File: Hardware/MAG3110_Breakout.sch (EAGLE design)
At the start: 17 parts, among them U1 MAG31101:1

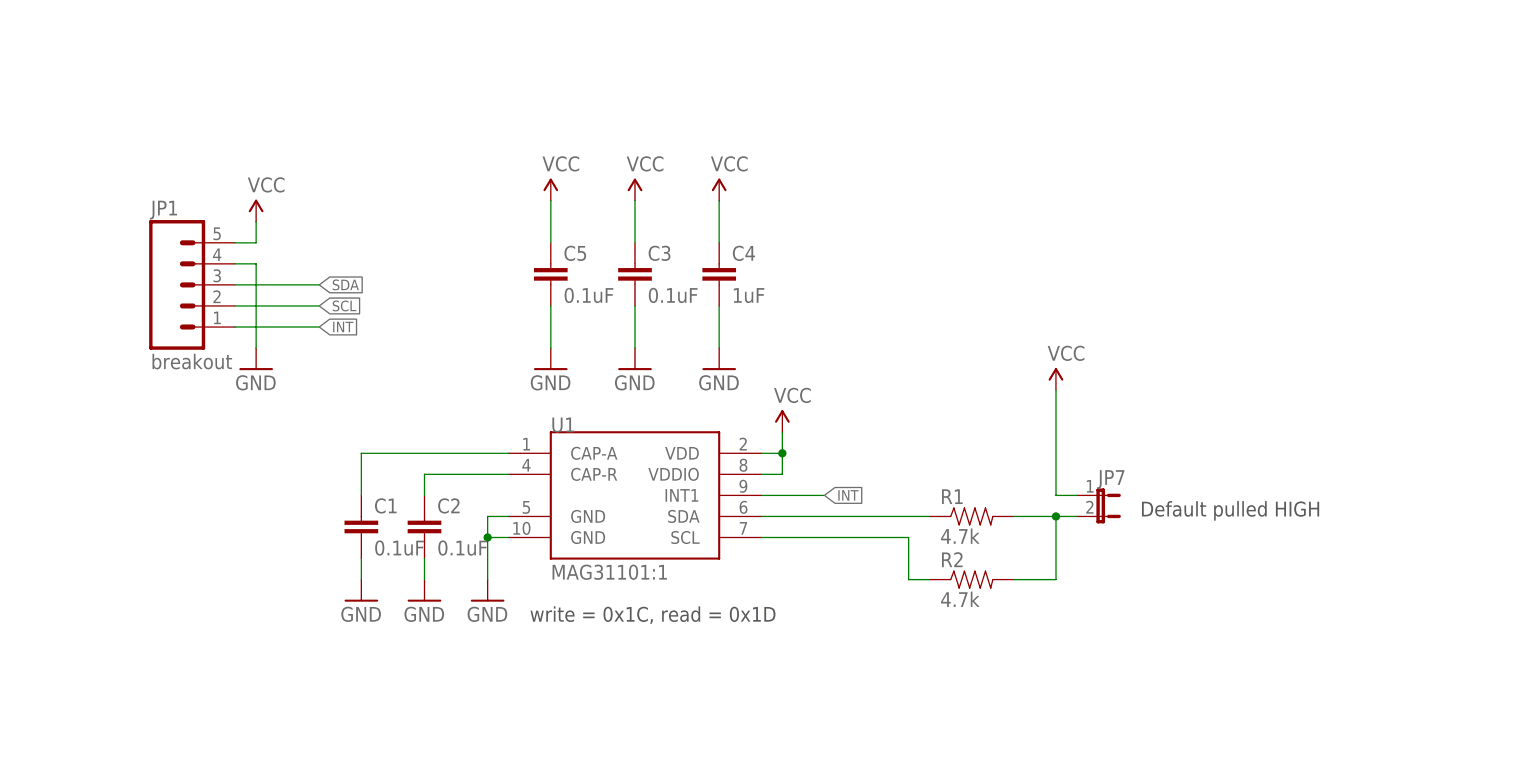
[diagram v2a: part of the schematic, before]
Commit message: Modified I2C pullup solder jumper
Changed solder jumper for I2C pullup so that I2C lines will be
completely floating if jumper is open. Moved capacitor bank to the left
.005 grid spaces and moved resistors and cap on right side over .005 to
the right, all for better trace routing. Changed int trace to be more
direct to header.
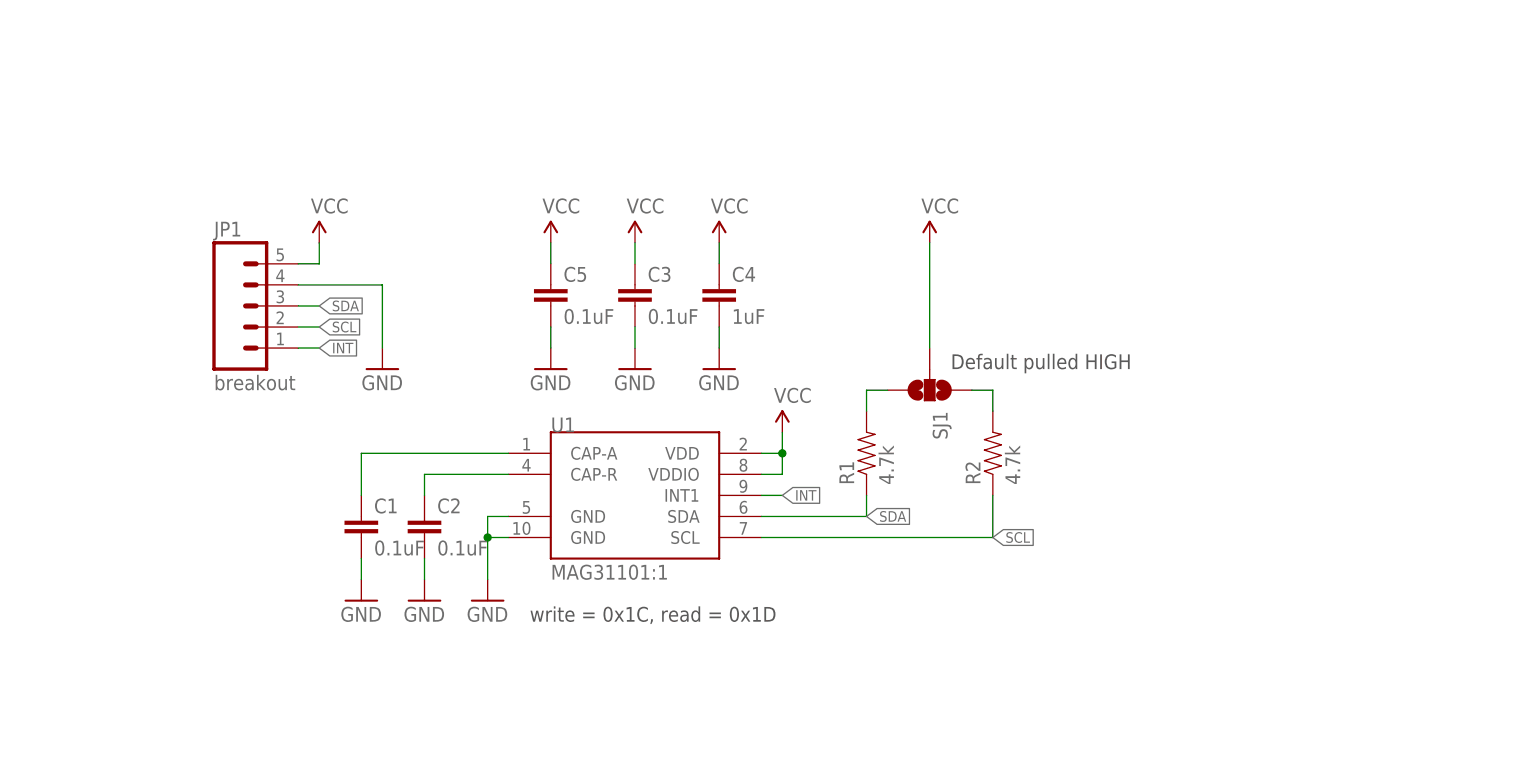
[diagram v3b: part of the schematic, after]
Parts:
- removed JP7: (no value), SparkFun-Passives:JUMPER-2SMD-NC
- added SJ1: (no value), SparkFun-Passives:SOLDERJUMPER_2WAYPASTE1&2&3
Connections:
- new net N$4: R1.2, SJ1.3
- net N$3: now also SJ1.1; no longer JP7.2, R1.2
- net VCC: now also SJ1.2; no longer JP7.1
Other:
- moved on the sheet: C3, C4, C5, JP1, R1, R2
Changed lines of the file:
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@@
 <?xml version="1.0" encoding="utf-8"?>
 <!DOCTYPE eagle SYSTEM "eagle.dtd">
-<eagle version="6.4">
+<eagle version="6.5.0">
 <drawing>
 <settings>
@@
 <part name="GND7" library="SparkFun" deviceset="GND" device=""/>
 <part name="GND8" library="SparkFun" deviceset="GND" device=""/>
-<part name="JP7" library="SparkFun-Passives" deviceset="JUMPER-2" device="SMD-NC"/>
+<part name="SJ1" library="SparkFun-Passives" deviceset="SOLDERJUMPER_2WAY" device="PASTE1&amp;2&amp;3"/>
 </parts>
 <sheets>
@@
 <text x="241.3" y="7.62" size="2.54" layer="94" ratio="15">12</text>
 <text x="167.64" y="10.16" size="2.54" layer="94" ratio="15">Kade Jensen</text>
-<text x="185.42" y="83.82" size="1.778" layer="97">Default pulled HIGH</text>
+<text x="162.56" y="101.6" size="1.778" layer="97">Default pulled HIGH</text>
 </plain>
 <instances>
@@
 <instance part="GND2" gate="1" x="91.44" y="73.66"/>
 <instance part="GND3" gate="1" x="99.06" y="73.66"/>
-<instance part="C3" gate="G$1" x="124.46" y="111.76"/>
-<instance part="C4" gate="G$1" x="134.62" y="111.76"/>
-<instance part="P+1" gate="1" x="124.46" y="121.92"/>
+<instance part="C3" gate="G$1" x="124.46" y="109.22"/>
+<instance part="C4" gate="G$1" x="134.62" y="109.22"/>
+<instance part="P+1" gate="1" x="124.46" y="116.84"/>
 <instance part="GND4" gate="1" x="124.46" y="101.6"/>
 <instance part="P+2" gate="1" x="142.24" y="93.98"/>
-<instance part="C5" gate="G$1" x="114.3" y="111.76"/>
-<instance part="R1" gate="G$1" x="165.1" y="83.82"/>
-<instance part="R2" gate="G$1" x="165.1" y="76.2"/>
-<instance part="P+3" gate="1" x="175.26" y="99.06"/>
-<instance part="JP1" gate="G$1" x="68.58" y="111.76"/>
-<instance part="P+4" gate="1" x="78.74" y="119.38"/>
-<instance part="GND5" gate="1" x="78.74" y="101.6"/>
+<instance part="C5" gate="G$1" x="114.3" y="109.22"/>
+<instance part="R1" gate="G$1" x="152.4" y="91.44" rot="R90"/>
+<instance part="R2" gate="G$1" x="167.64" y="91.44" rot="R90"/>
+<instance part="P+3" gate="1" x="160.02" y="116.84"/>
+<instance part="JP1" gate="G$1" x="76.2" y="109.22"/>
+<instance part="P+4" gate="1" x="86.36" y="116.84"/>
+<instance part="GND5" gate="1" x="93.98" y="101.6"/>
 <instance part="JP2" gate="G$1" x="246.38" y="25.4"/>
 <instance part="JP3" gate="G$1" x="246.38" y="33.02"/>
@@
 <instance part="FRAME2" gate="G$2" x="147.32" y="0"/>
 <instance part="LOGO1" gate="G$1" x="15.24" y="12.7"/>
-<instance part="P+5" gate="1" x="114.3" y="121.92"/>
-<instance part="P+6" gate="1" x="134.62" y="121.92"/>
+<instance part="P+5" gate="1" x="114.3" y="116.84"/>
+<instance part="P+6" gate="1" x="134.62" y="116.84"/>
 <instance part="GND7" gate="1" x="114.3" y="101.6"/>
 <instance part="GND8" gate="1" x="134.62" y="101.6"/>
-<instance part="JP7" gate="A" x="180.34" y="86.36" rot="R270"/>
+<instance part="SJ1" gate="G$1" x="160.02" y="99.06" rot="R270"/>
 </instances>
 <busses>
@@
 </segment>
 <segment>
-<wire x1="124.46" y1="104.14" x2="124.46" y2="109.22" width="0.1524" layer="91"/>
+<wire x1="124.46" y1="104.14" x2="124.46" y2="106.68" width="0.1524" layer="91"/>
 <pinref part="C3" gate="G$1" pin="2"/>
 <pinref part="GND4" gate="1" pin="GND"/>
 </segment>
 <segment>
-<wire x1="76.2" y1="114.3" x2="78.74" y2="114.3" width="0.1524" layer="91"/>
-<wire x1="78.74" y1="114.3" x2="78.74" y2="104.14" width="0.1524" layer="91"/>
+<wire x1="83.82" y1="111.76" x2="93.98" y2="111.76" width="0.1524" layer="91"/>
+<wire x1="93.98" y1="111.76" x2="93.98" y2="104.14" width="0.1524" layer="91"/>
 <pinref part="JP1" gate="G$1" pin="4"/>
 <pinref part="GND5" gate="1" pin="GND"/>
@@
 <pinref part="C4" gate="G$1" pin="2"/>
 <pinref part="GND8" gate="1" pin="GND"/>
-<wire x1="134.62" y1="109.22" x2="134.62" y2="104.14" width="0.1524" layer="91"/>
+<wire x1="134.62" y1="106.68" x2="134.62" y2="104.14" width="0.1524" layer="91"/>
 </segment>
 <segment>
 <pinref part="C5" gate="G$1" pin="2"/>
 <pinref part="GND7" gate="1" pin="GND"/>
-<wire x1="114.3" y1="109.22" x2="114.3" y2="104.14" width="0.1524" layer="91"/>
+<wire x1="114.3" y1="106.68" x2="114.3" y2="104.14" width="0.1524" layer="91"/>
 </segment>
 </net>
 <net name="VCC" class="0">
 <segment>
-<wire x1="124.46" y1="121.92" x2="124.46" y2="116.84" width="0.1524" layer="91"/>
+<wire x1="124.46" y1="116.84" x2="124.46" y2="114.3" width="0.1524" layer="91"/>
 <pinref part="C3" gate="G$1" pin="1"/>
 <pinref part="P+1" gate="1" pin="VCC"/>
@@
 </segment>
 <segment>
-<wire x1="76.2" y1="116.84" x2="78.74" y2="116.84" width="0.1524" layer="91"/>
-<wire x1="78.74" y1="116.84" x2="78.74" y2="119.38" width="0.1524" layer="91"/>
+<wire x1="83.82" y1="114.3" x2="86.36" y2="114.3" width="0.1524" layer="91"/>
+<wire x1="86.36" y1="114.3" x2="86.36" y2="116.84" width="0.1524" layer="91"/>
 <pinref part="JP1" gate="G$1" pin="5"/>
 <pinref part="P+4" gate="1" pin="VCC"/>
@@
 <segment>
 <pinref part="P+3" gate="1" pin="VCC"/>
-<wire x1="175.26" y1="86.36" x2="175.26" y2="99.06" width="0.1524" layer="91"/>
-<pinref part="JP7" gate="A" pin="1"/>
-<wire x1="177.8" y1="86.36" x2="175.26" y2="86.36" width="0.1524" layer="91"/>
+<wire x1="160.02" y1="104.14" x2="160.02" y2="116.84" width="0.1524" layer="91"/>
+<pinref part="SJ1" gate="G$1" pin="2"/>
 </segment>
 <segment>
 <pinref part="C5" gate="G$1" pin="1"/>
 <pinref part="P+5" gate="1" pin="VCC"/>
-<wire x1="114.3" y1="116.84" x2="114.3" y2="121.92" width="0.1524" layer="91"/>
+<wire x1="114.3" y1="114.3" x2="114.3" y2="116.84" width="0.1524" layer="91"/>
 </segment>
 <segment>
 <pinref part="C4" gate="G$1" pin="1"/>
 <pinref part="P+6" gate="1" pin="VCC"/>
-<wire x1="134.62" y1="121.92" x2="134.62" y2="116.84" width="0.1524" layer="91"/>
+<wire x1="134.62" y1="116.84" x2="134.62" y2="114.3" width="0.1524" layer="91"/>
 </segment>
 </net>
 <net name="SDA" class="0">
 <segment>
-<wire x1="139.7" y1="83.82" x2="160.02" y2="83.82" width="0.1524" layer="91"/>
+<wire x1="83.82" y1="109.22" x2="86.36" y2="109.22" width="0.1524" layer="91"/>
+<pinref part="JP1" gate="G$1" pin="3"/>
+<label x="86.36" y="109.22" size="1.27" layer="95" xref="yes"/>
+</segment>
+<segment>
+<pinref part="R1" gate="G$1" pin="1"/>
+<wire x1="152.4" y1="86.36" x2="152.4" y2="83.82" width="0.1524" layer="91"/>
 <pinref part="U1" gate="G$1" pin="SDA"/>
-<pinref part="R1" gate="G$1" pin="1"/>
-</segment>
-<segment>
-<wire x1="76.2" y1="111.76" x2="86.36" y2="111.76" width="0.1524" layer="91"/>
-<pinref part="JP1" gate="G$1" pin="3"/>
-<label x="86.36" y="111.76" size="1.27" layer="95" xref="yes"/>
+<wire x1="152.4" y1="83.82" x2="139.7" y2="83.82" width="0.1524" layer="91"/>
+<label x="152.4" y="83.82" size="1.27" layer="95" xref="yes"/>
 </segment>
 </net>
 <net name="SCL" class="0">
 <segment>
-<wire x1="157.48" y1="76.2" x2="160.02" y2="76.2" width="0.1524" layer="91"/>
+<wire x1="167.64" y1="81.28" x2="167.64" y2="86.36" width="0.1524" layer="91"/>
 <pinref part="R2" gate="G$1" pin="1"/>
 <pinref part="U1" gate="G$1" pin="SCL"/>
-<wire x1="139.7" y1="81.28" x2="157.48" y2="81.28" width="0.1524" layer="91"/>
-<wire x1="157.48" y1="81.28" x2="157.48" y2="76.2" width="0.1524" layer="91"/>
-</segment>
-<segment>
-<wire x1="76.2" y1="109.22" x2="86.36" y2="109.22" width="0.1524" layer="91"/>
+<wire x1="139.7" y1="81.28" x2="167.64" y2="81.28" width="0.1524" layer="91"/>
+<label x="167.64" y="81.28" size="1.27" layer="95" xref="yes"/>
+</segment>
+<segment>
+<wire x1="83.82" y1="106.68" x2="86.36" y2="106.68" width="0.1524" layer="91"/>
 <pinref part="JP1" gate="G$1" pin="2"/>
-<label x="86.36" y="109.22" size="1.27" layer="95" xref="yes"/>
+<label x="86.36" y="106.68" size="1.27" layer="95" xref="yes"/>
 </segment>
 </net>
 <net name="INT" class="0">
 <segment>
-<wire x1="139.7" y1="86.36" x2="147.32" y2="86.36" width="0.1524" layer="91"/>
+<wire x1="139.7" y1="86.36" x2="142.24" y2="86.36" width="0.1524" layer="91"/>
 <pinref part="U1" gate="G$1" pin="INT1"/>
-<label x="147.32" y="86.36" size="1.27" layer="95" xref="yes"/>
-</segment>
-<segment>
-<wire x1="76.2" y1="106.68" x2="86.36" y2="106.68" width="0.1524" layer="91"/>
+<label x="142.24" y="86.36" size="1.27" layer="95" xref="yes"/>
+</segment>
+<segment>
+<wire x1="83.82" y1="104.14" x2="86.36" y2="104.14" width="0.1524" layer="91"/>
 <pinref part="JP1" gate="G$1" pin="1"/>
-<label x="86.36" y="106.68" size="1.27" layer="95" xref="yes"/>
+<label x="86.36" y="104.14" size="1.27" layer="95" xref="yes"/>
 </segment>
 </net>
@@
 <segment>
 <pinref part="R2" gate="G$1" pin="2"/>
-<wire x1="170.18" y1="76.2" x2="175.26" y2="76.2" width="0.1524" layer="91"/>
+<wire x1="167.64" y1="96.52" x2="167.64" y2="99.06" width="0.1524" layer="91"/>
+<pinref part="SJ1" gate="G$1" pin="1"/>
+<wire x1="167.64" y1="99.06" x2="165.1" y2="99.06" width="0.1524" layer="91"/>
+</segment>
+</net>
+<net name="N$4" class="0">
+<segment>
 <pinref part="R1" gate="G$1" pin="2"/>
-<wire x1="170.18" y1="83.82" x2="175.26" y2="83.82" width="0.1524" layer="91"/>
-<pinref part="JP7" gate="A" pin="2"/>
-<wire x1="175.26" y1="83.82" x2="177.8" y2="83.82" width="0.1524" layer="91"/>
-<wire x1="175.26" y1="76.2" x2="175.26" y2="83.82" width="0.1524" layer="91"/>
-<junction x="175.26" y="83.82"/>
-</segment>
-</net>
+<wire x1="152.4" y1="96.52" x2="152.4" y2="99.06" width="0.1524" layer="91"/>
+<pinref part="SJ1" gate="G$1" pin="3"/>
+<wire x1="154.94" y1="99.06" x2="152.4" y2="99.06" width="0.1524" layer="91"/>
+</segment>
+</net>

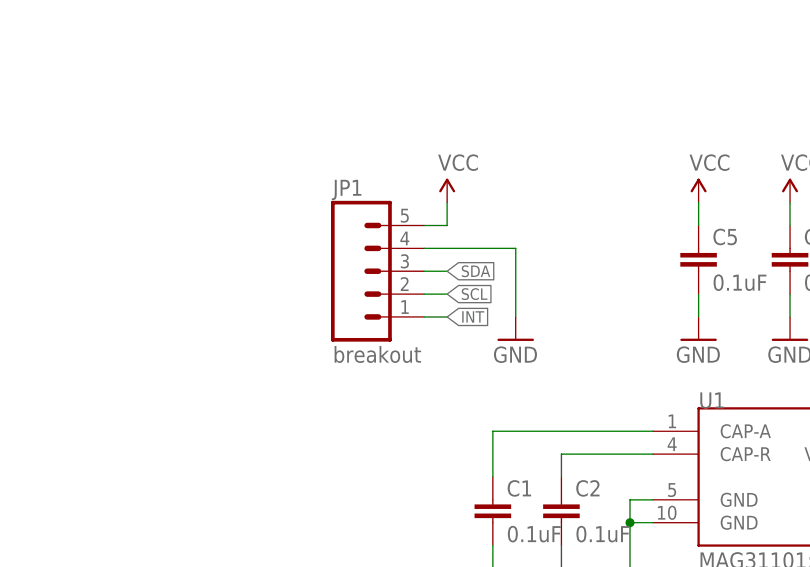
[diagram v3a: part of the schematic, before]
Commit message: Reordered Pinout
1.) Reordered pinout to adhere to new I2C layout standard
2.) Added "fake trace" to NC leg of IC for more uniform heat
distribution.
3.) Minor trace efficiency edits
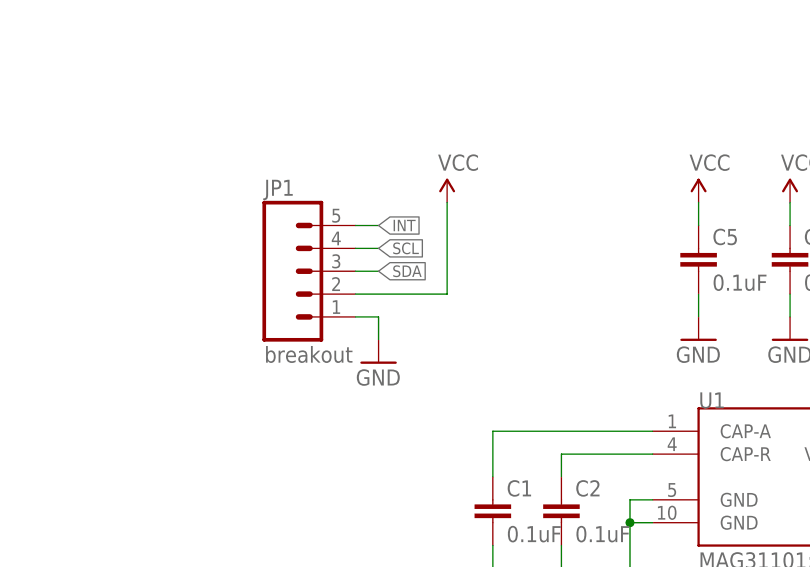
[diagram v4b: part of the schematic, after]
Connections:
- net GND: now also JP1.1; no longer JP1.4
- net INT: now also JP1.5; no longer JP1.1
- net SCL: now also JP1.4; no longer JP1.2
- net VCC: now also JP1.2; no longer JP1.5
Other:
- moved on the sheet: JP1
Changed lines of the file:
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@@
 <instance part="R2" gate="G$1" x="167.64" y="91.44" rot="R90"/>
 <instance part="P+3" gate="1" x="160.02" y="116.84"/>
-<instance part="JP1" gate="G$1" x="76.2" y="109.22"/>
+<instance part="JP1" gate="G$1" x="68.58" y="109.22"/>
 <instance part="P+4" gate="1" x="86.36" y="116.84"/>
-<instance part="GND5" gate="1" x="93.98" y="101.6"/>
+<instance part="GND5" gate="1" x="78.74" y="99.06"/>
 <instance part="JP2" gate="G$1" x="246.38" y="25.4"/>
 <instance part="JP3" gate="G$1" x="246.38" y="33.02"/>
@@
 </segment>
 <segment>
-<wire x1="83.82" y1="111.76" x2="93.98" y2="111.76" width="0.1524" layer="91"/>
-<wire x1="93.98" y1="111.76" x2="93.98" y2="104.14" width="0.1524" layer="91"/>
-<pinref part="JP1" gate="G$1" pin="4"/>
-<pinref part="GND5" gate="1" pin="GND"/>
-</segment>
-<segment>
 <pinref part="C4" gate="G$1" pin="2"/>
 <pinref part="GND8" gate="1" pin="GND"/>
@@
 <pinref part="GND7" gate="1" pin="GND"/>
 <wire x1="114.3" y1="106.68" x2="114.3" y2="104.14" width="0.1524" layer="91"/>
+</segment>
+<segment>
+<pinref part="JP1" gate="G$1" pin="1"/>
+<pinref part="GND5" gate="1" pin="GND"/>
+<wire x1="76.2" y1="104.14" x2="78.74" y2="104.14" width="0.1524" layer="91"/>
+<wire x1="78.74" y1="104.14" x2="78.74" y2="101.6" width="0.1524" layer="91"/>
 </segment>
 </net>
@@
 </segment>
 <segment>
-<wire x1="83.82" y1="114.3" x2="86.36" y2="114.3" width="0.1524" layer="91"/>
-<wire x1="86.36" y1="114.3" x2="86.36" y2="116.84" width="0.1524" layer="91"/>
-<pinref part="JP1" gate="G$1" pin="5"/>
-<pinref part="P+4" gate="1" pin="VCC"/>
-</segment>
-<segment>
 <pinref part="P+3" gate="1" pin="VCC"/>
 <wire x1="160.02" y1="104.14" x2="160.02" y2="116.84" width="0.1524" layer="91"/>
@@
 <wire x1="134.62" y1="116.84" x2="134.62" y2="114.3" width="0.1524" layer="91"/>
 </segment>
+<segment>
+<pinref part="JP1" gate="G$1" pin="2"/>
+<wire x1="76.2" y1="106.68" x2="86.36" y2="106.68" width="0.1524" layer="91"/>
+<wire x1="86.36" y1="106.68" x2="86.36" y2="116.84" width="0.1524" layer="91"/>
+<pinref part="P+4" gate="1" pin="VCC"/>
+</segment>
 </net>
 <net name="SDA" class="0">
-<segment>
-<wire x1="83.82" y1="109.22" x2="86.36" y2="109.22" width="0.1524" layer="91"/>
-<pinref part="JP1" gate="G$1" pin="3"/>
-<label x="86.36" y="109.22" size="1.27" layer="95" xref="yes"/>
-</segment>
 <segment>
 <pinref part="R1" gate="G$1" pin="1"/>
@@
 <wire x1="152.4" y1="83.82" x2="139.7" y2="83.82" width="0.1524" layer="91"/>
 <label x="152.4" y="83.82" size="1.27" layer="95" xref="yes"/>
+</segment>
+<segment>
+<pinref part="JP1" gate="G$1" pin="3"/>
+<wire x1="76.2" y1="109.22" x2="78.74" y2="109.22" width="0.1524" layer="91"/>
+<label x="78.74" y="109.22" size="1.27" layer="95" xref="yes"/>
 </segment>
 </net>
@@
 </segment>
 <segment>
-<wire x1="83.82" y1="106.68" x2="86.36" y2="106.68" width="0.1524" layer="91"/>
-<pinref part="JP1" gate="G$1" pin="2"/>
-<label x="86.36" y="106.68" size="1.27" layer="95" xref="yes"/>
+<pinref part="JP1" gate="G$1" pin="4"/>
+<wire x1="76.2" y1="111.76" x2="78.74" y2="111.76" width="0.1524" layer="91"/>
+<label x="78.74" y="111.76" size="1.27" layer="95" xref="yes"/>
 </segment>
 </net>
@@
 </segment>
 <segment>
-<wire x1="83.82" y1="104.14" x2="86.36" y2="104.14" width="0.1524" layer="91"/>
-<pinref part="JP1" gate="G$1" pin="1"/>
-<label x="86.36" y="104.14" size="1.27" layer="95" xref="yes"/>
+<pinref part="JP1" gate="G$1" pin="5"/>
+<wire x1="76.2" y1="114.3" x2="78.74" y2="114.3" width="0.1524" layer="91"/>
+<label x="78.74" y="114.3" size="1.27" layer="95" xref="yes"/>
 </segment>
 </net>
